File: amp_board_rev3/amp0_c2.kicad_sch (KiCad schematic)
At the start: 28 parts, among them U10 SMCJ150A, U7 SMCJ150A, U8 PA343, U9 PA343

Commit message: routing complete
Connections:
- net GND: now also U9.25 (EPAD), U9.26, U9.27
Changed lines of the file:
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@@
 	)
 	(junction
+		(at 182.88 95.25)
+		(diameter 0)
+		(color 0 0 0 0)
+	)
+	(junction
 		(at 278.13 127)
 		(diameter 0)
@@
 	(wire
 		(pts
+			(xy 182.88 95.25) (xy 182.88 102.87)
+		)
+		(stroke
+			(width 0)
+			(type default)
+		)
+	)
+	(wire
+		(pts
 			(xy 50.8 78.74) (xy 152.4 78.74)
 		)
@@
 	(wire
 		(pts
+			(xy 182.88 93.98) (xy 182.88 95.25)
+		)
+		(stroke
+			(width 0)
+			(type default)
+		)
+	)
+	(wire
+		(pts
 			(xy 266.7 52.07) (xy 252.73 52.07)
 		)
@@
 	(wire
 		(pts
+			(xy 185.42 93.98) (xy 182.88 93.98)
+		)
+		(stroke
+			(width 0)
+			(type default)
+		)
+	)
+	(wire
+		(pts
 			(xy 300.99 127) (xy 285.75 127)
 		)
@@
 	(symbol
 		(lib_id "power:GND")
-		(at 182.88 95.25 0)
+		(at 182.88 102.87 0)
 		(unit 1)
 		(exclude_from_sim no)
@@
 		(fields_autoplaced yes)
 		(property "Reference" "#PWR033"
-			(at 182.88 101.6 0)
+			(at 182.88 109.22 0)
 			(effects
 				(font
@@
 		)
 		(property "Value" "GND"
-			(at 182.88 100.33 0)
+			(at 182.88 107.95 0)
 			(effects
 				(font
@@
 		)
 		(property "Footprint" ""
-			(at 182.88 95.25 0)
+			(at 182.88 102.87 0)
 			(effects
 				(font
@@
 		)
 		(property "Datasheet" ""
-			(at 182.88 95.25 0)
+			(at 182.88 102.87 0)
 			(effects
 				(font
@@
 		)
 		(property "Description" "Power symbol creates a global label with name \"GND\" , ground"
-			(at 182.88 95.25 0)
+			(at 182.88 102.87 0)
 			(effects
 				(font

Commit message: all routed
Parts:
- added R46, R48: 10, Resistor_SMD:R_0603_1608Metric, symbol Device:R_US
- added R47, R49: 100, Resistor_SMD:R_0603_1608Metric, symbol Device:R_US
- renumbered C19 to C31, C20 to C32, C21 to C33, C22 to C34, C26 to C38, R14 to R26, R15 to R27, R16 to R28, R17 to R29, R18 to R30, R19 to R31, U7 to U13, U8 to U14, U9 to U15
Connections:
- net GND: now also R47.1, R49.1; no longer C25.2, C33.2, C34.2 (-), C38.2 (-), U10.2 (A), U13.2 (A), U14.12, U14.24, U14.25 (EPAD), U14.26, U14.27, U14.9 (+IN_B), U15.24, U15.25 (EPAD), U15.26, U15.27, U9.12, U9.9 (+IN_B)
- net input_4a_lv: now also R46.1, R47.2; no longer C15.2
- net input_5a_lv: now also R48.1, R49.2; no longer C16.2
- new net: C15.2, R46.2
- new net: C16.2, R48.2
- new net VSS: C25.2, C33.2, C34.2 (-), C38.2 (-), U10.2 (A), U13.2 (A), U14.12, U14.24, U14.25 (EPAD), U14.26, U14.27, U14.9 (+IN_B), U15.24, U15.25 (EPAD), U15.26, U15.27, U9.12, U9.9 (+IN_B)

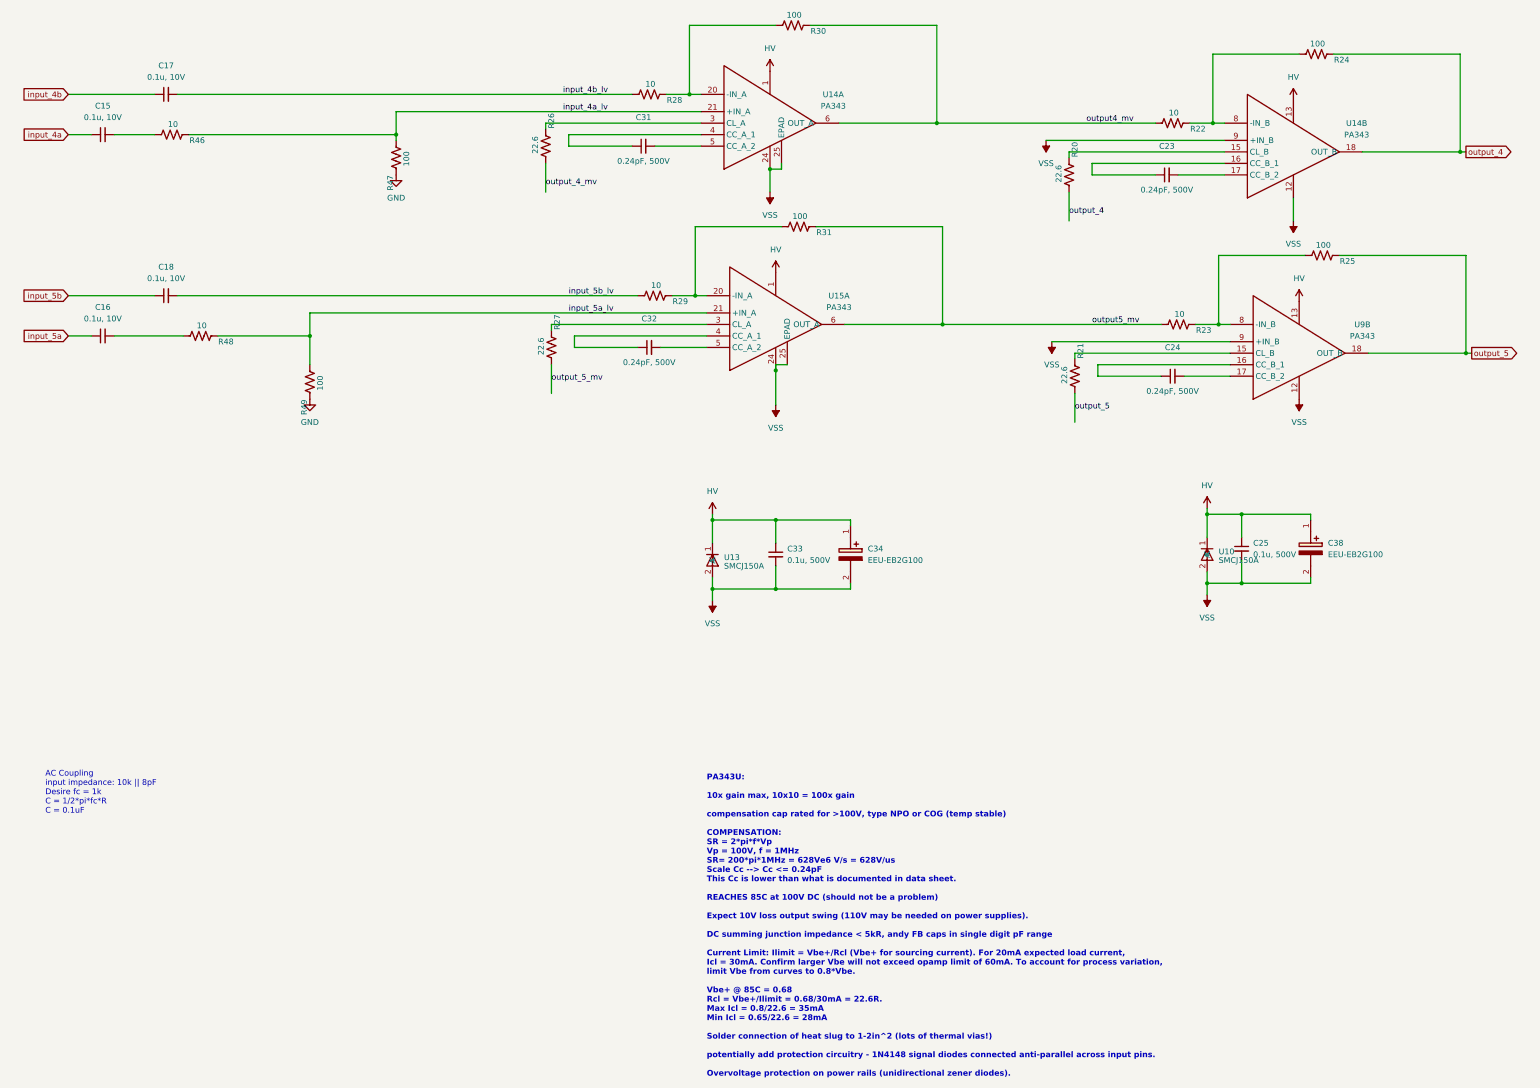
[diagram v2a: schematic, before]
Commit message: updated ground references in schematic
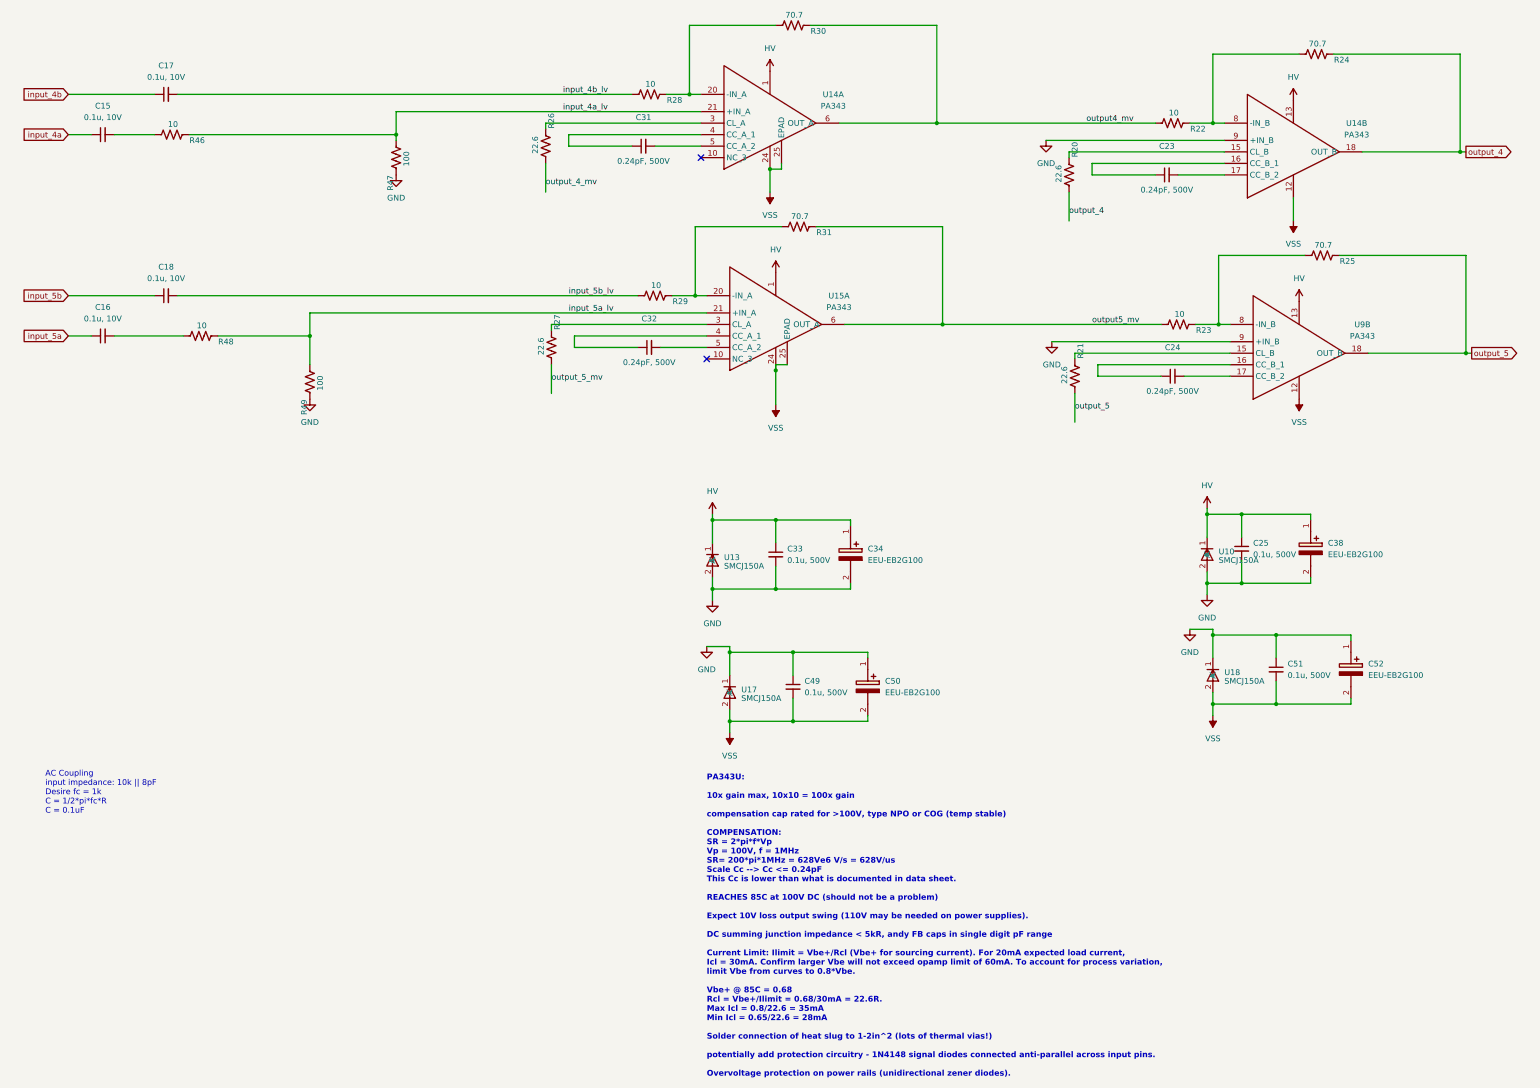
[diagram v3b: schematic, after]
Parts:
- added C49, C51: 0.1u, 500V, Capacitor_SMD:C_1812_4532Metric, symbol Device:C_Small
- added C50, C52: EEU-EB2G100, 726_footprints:EEU-EB2G100, symbol _PHASE:EEU-EB2G100
- added U17, U18: SMCJ150A, 726_footprints:SMCJ150A-13-F, symbol _PHASE:SMCJ150A-13-F
- R24, R25, R30, R31: value 100 -> 70.7
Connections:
- net GND: now also C25.2, C33.2, C34.2 (-), C38.2 (-), U10.2 (A), U13.2 (A), U14.9 (+IN_B), U9.9 (+IN_B), C49.1, C50.1 (+), C51.1, C52.1 (+), U17.1 (K), U18.1 (K)
- net VSS: now also C49.2, C50.2 (-), C51.2, C52.2 (-), U17.2 (A), U18.2 (A); no longer C25.2, C33.2, C34.2 (-), C38.2 (-), U10.2 (A), U13.2 (A), U14.9 (+IN_B), U9.9 (+IN_B)
- no-connect marks 0 -> 2

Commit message: updates based on 11/14 meeting
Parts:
- C15, C16, C17, C18: footprint Capacitor_SMD:C_0603_1608Metric -> (none)
- C23, C24: value 0.24pF, 500V -> 0.2pF, 250V; footprint Capacitor_SMD:C_0402_1005Metric -> (none)
- C25, C33, C49, C51: footprint Capacitor_SMD:C_1812_4532Metric -> (none)
- C31, C32: value 0.24pF, 500V -> 0.75pF, 250V; footprint Capacitor_SMD:C_0402_1005Metric -> (none)
- C34, C38, C50, C52: footprint 726_footprints:EEU-EB2G100 -> CAPPRD500W65D1000H2200
- R20, R21, R22, R23, R24, R25, R26, R27, R28, R29, R30, R31, R46, R47, R48, R49: footprint Resistor_SMD:R_0603_1608Metric -> (none)
- U14, U15: footprint 726_footprints:PA341DF -> (none)
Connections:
- now unconnected: U14.10 (NC_3), U14.11 (NC_4), U14.14 (NC_5), U14.7 (NC_2), U15.10 (NC_3), U15.11 (NC_4), U15.14 (NC_5), U15.7 (NC_2)

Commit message: detailed adjustments
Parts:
- removed unit 2 of U14
- removed U9: PA343, 726_footprints:PA341DF, symbol _PHASE:PA343_2Units
- added unit 2 of U14
- added unit 2 of U15
- C15, C16, C17, C18: footprint (none) -> Capacitor_SMD:C_0603_1608Metric
- C23, C24, C31, C32: footprint (none) -> Capacitor_SMD:C_0805_2012Metric
- C25, C33, C49, C51: footprint (none) -> Capacitor_SMD:C_1812_4532Metric
- C34, C38, C50, C52: footprint CAPPRD500W65D1000H2200 -> 726_footprints:EEU-EB2G100
- U14, U15: footprint (none) -> 726_footprints:PA341DF
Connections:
- net GND: now also U14.9 (+IN_B), U15.9 (+IN_B)
- net HV: now also U14.13, U15.13
- net VSS: now also U14.12, U15.12
- net output_4: now also U14.18 (OUT_B)
- net output_5: now also U15.18 (OUT_B)
- net at R21.1: now also U15.15 (CL_B)
- net at R20.1: now also U14.15 (CL_B)
- net at C23.1: now also U14.16 (CC_B_1)
- net at C23.2: now also U14.17 (CC_B_2)
- net at R23.1, R25.2: now also U15.8 (-IN_B)
- net at C24.1: now also U15.16 (CC_B_1)
- net at C24.2: now also U15.17 (CC_B_2)
- net at R22.1, R24.2: now also U14.8 (-IN_B)
- no-connect marks 2 -> 16

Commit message: final fabrication generated
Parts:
- R22, R23, R28, R29, R46, R48: value 10 -> 100
- R24, R25, R30, R31: value 70.7 -> 707
- R47, R49: value 100 -> 707
